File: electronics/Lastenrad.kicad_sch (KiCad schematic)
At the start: 42 parts, among them J1 Conn_Coaxial_Power, J2 Conn_Coaxial_Power, J3 Conn_Coaxial_Power

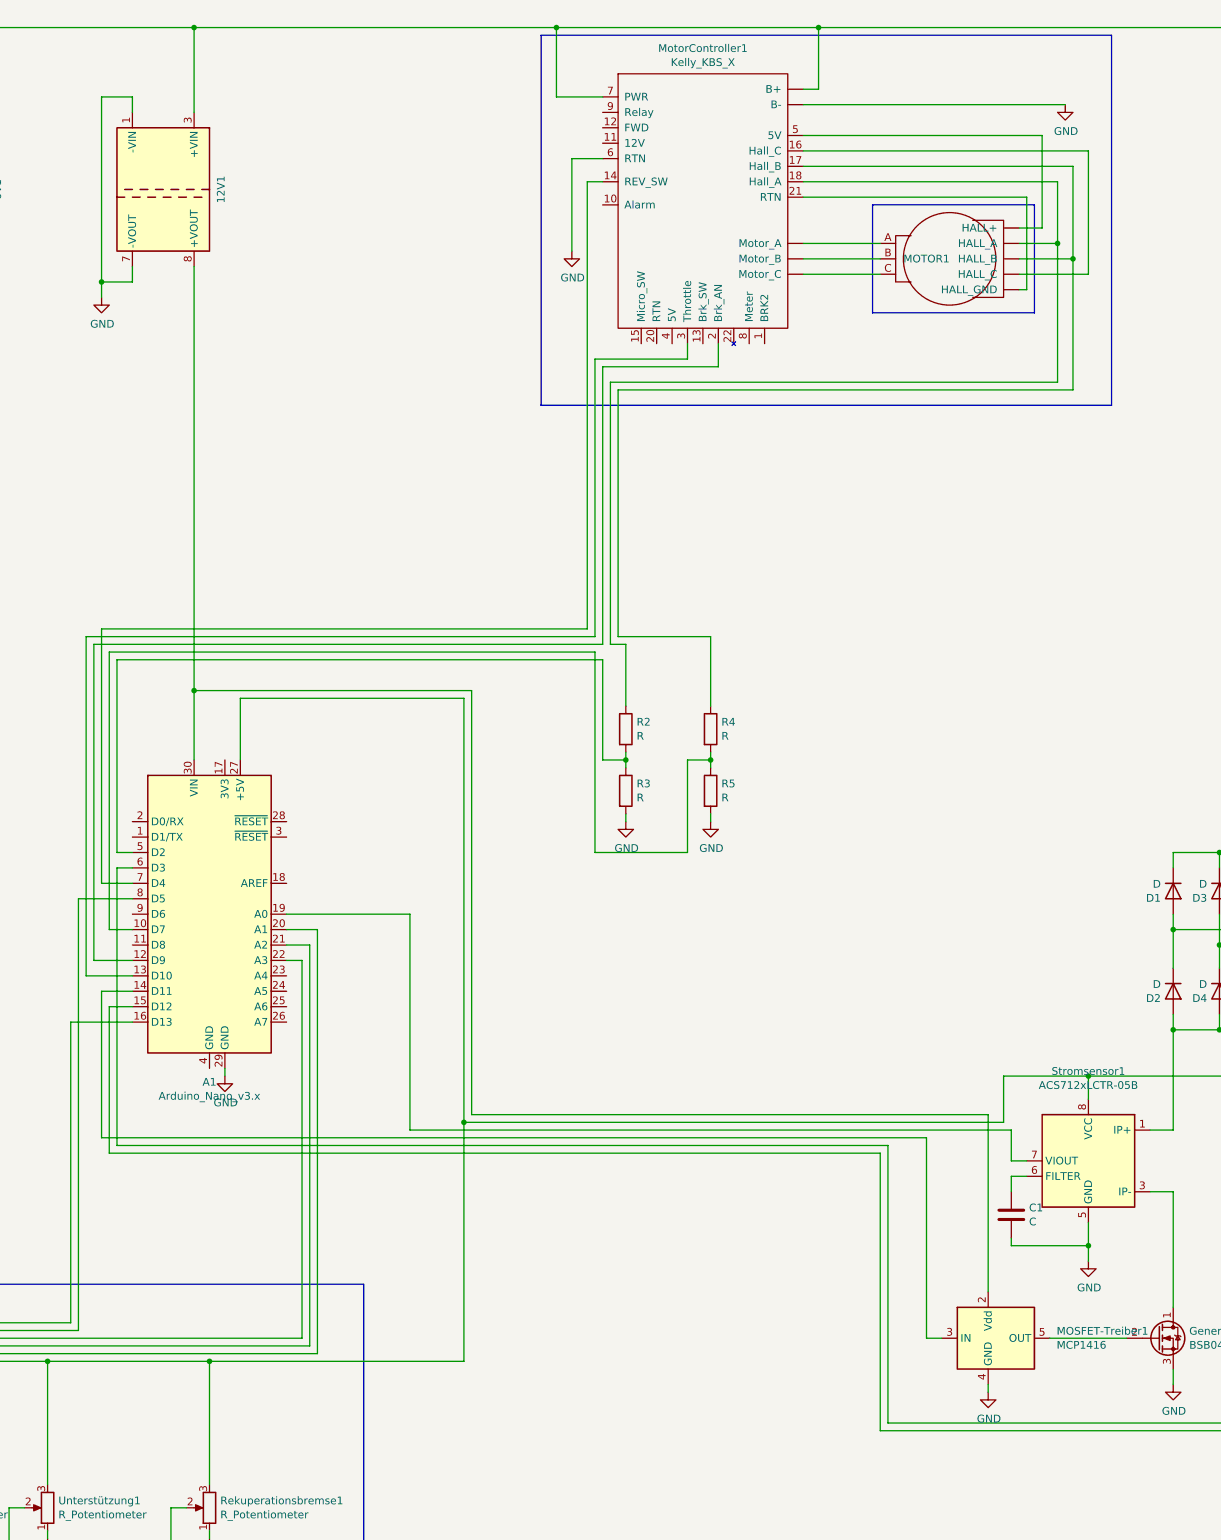
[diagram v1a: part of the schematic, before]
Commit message: Circuit diagram: Moved motor and motor controller
Slight adjustments to the positioning to make the connection between
different physical section more clear
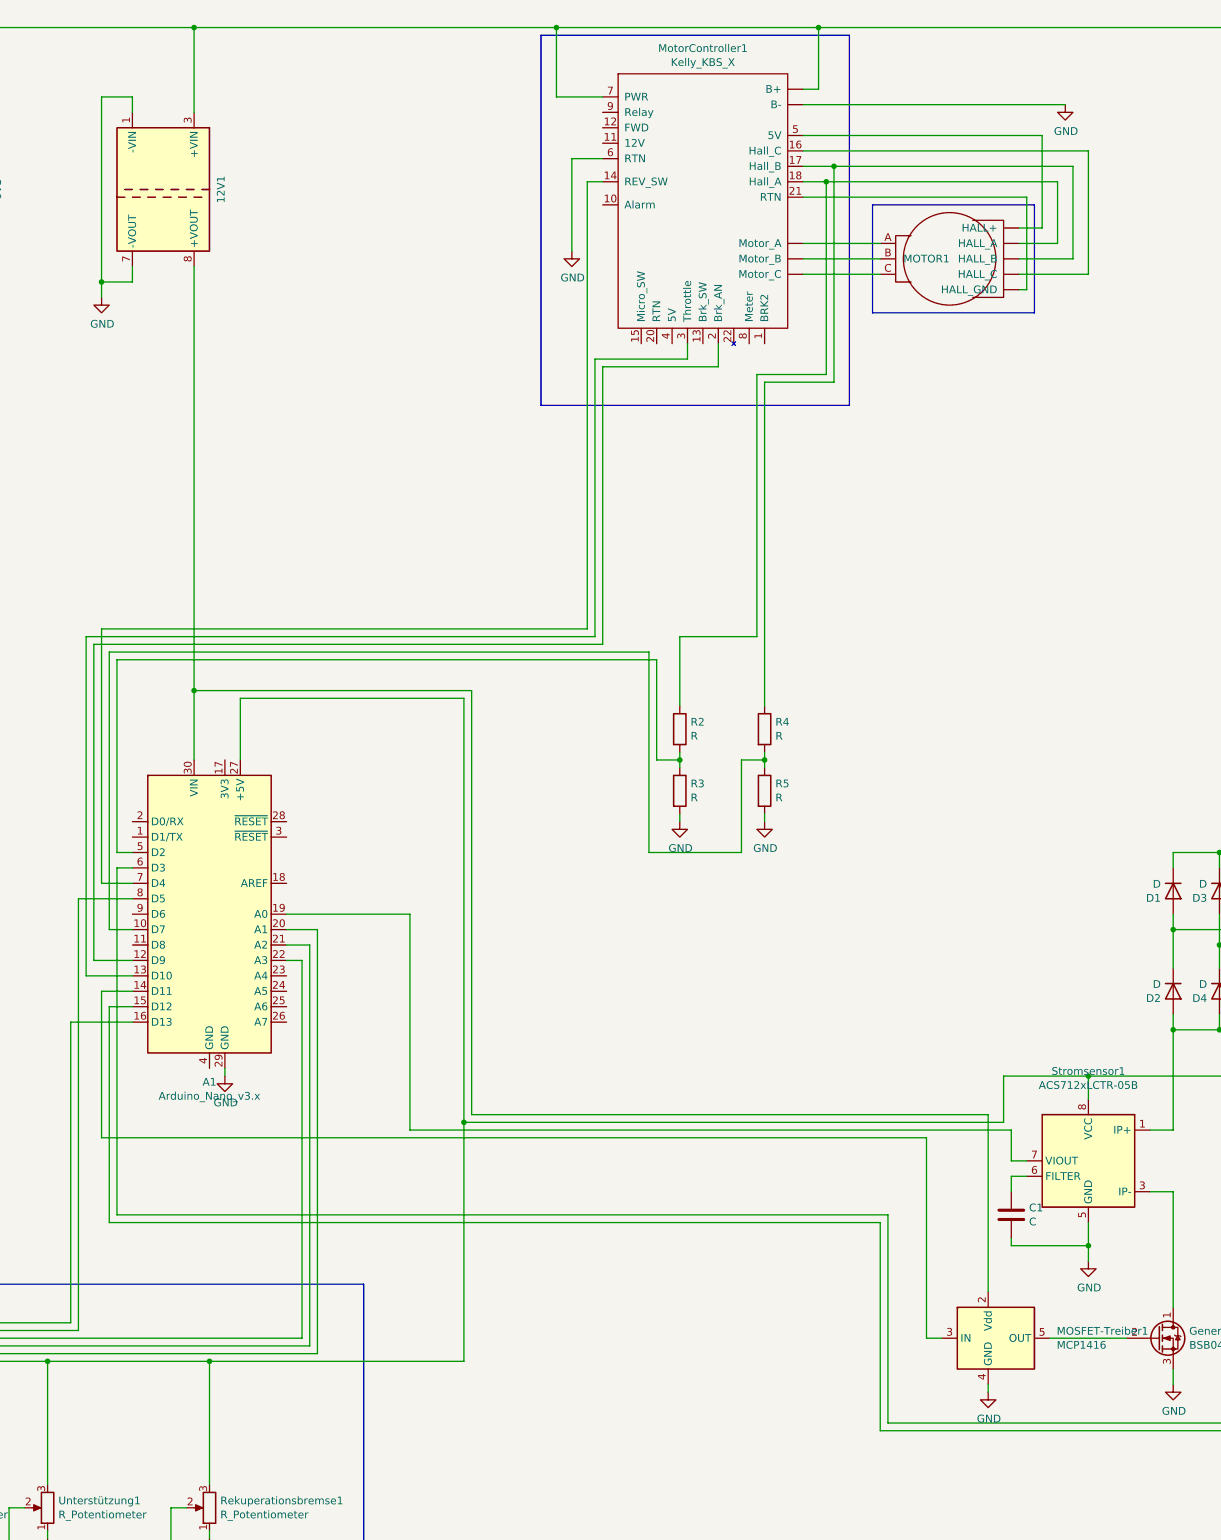
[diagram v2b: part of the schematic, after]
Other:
- moved on the sheet: R2, R3, R4, R5

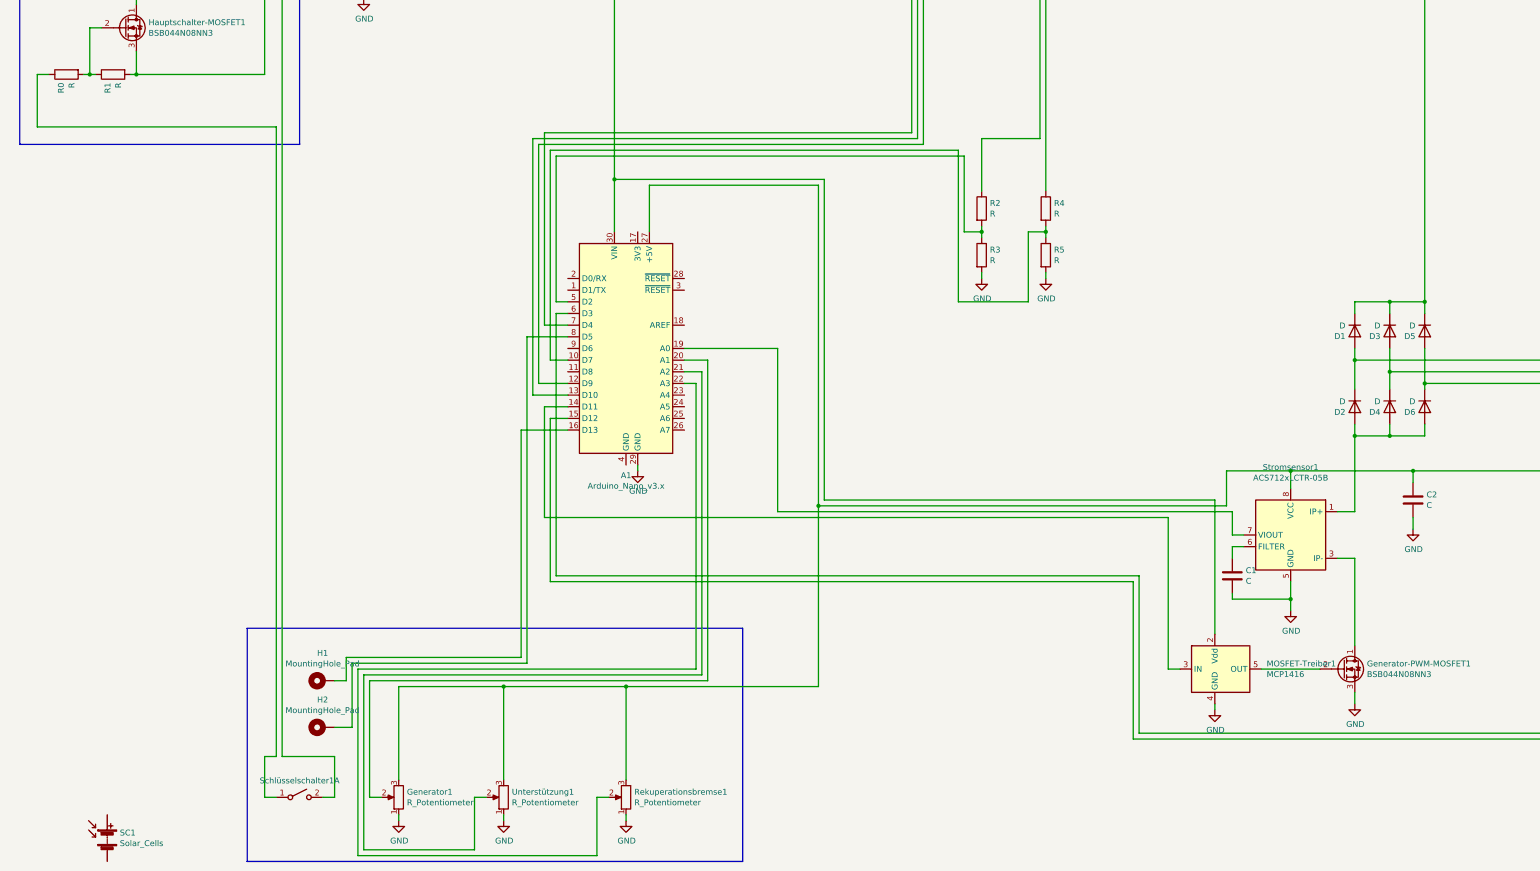
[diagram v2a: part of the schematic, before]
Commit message: Circuit diagram: Resistor values
My dad added sensible resistor values all around the circuit diagram
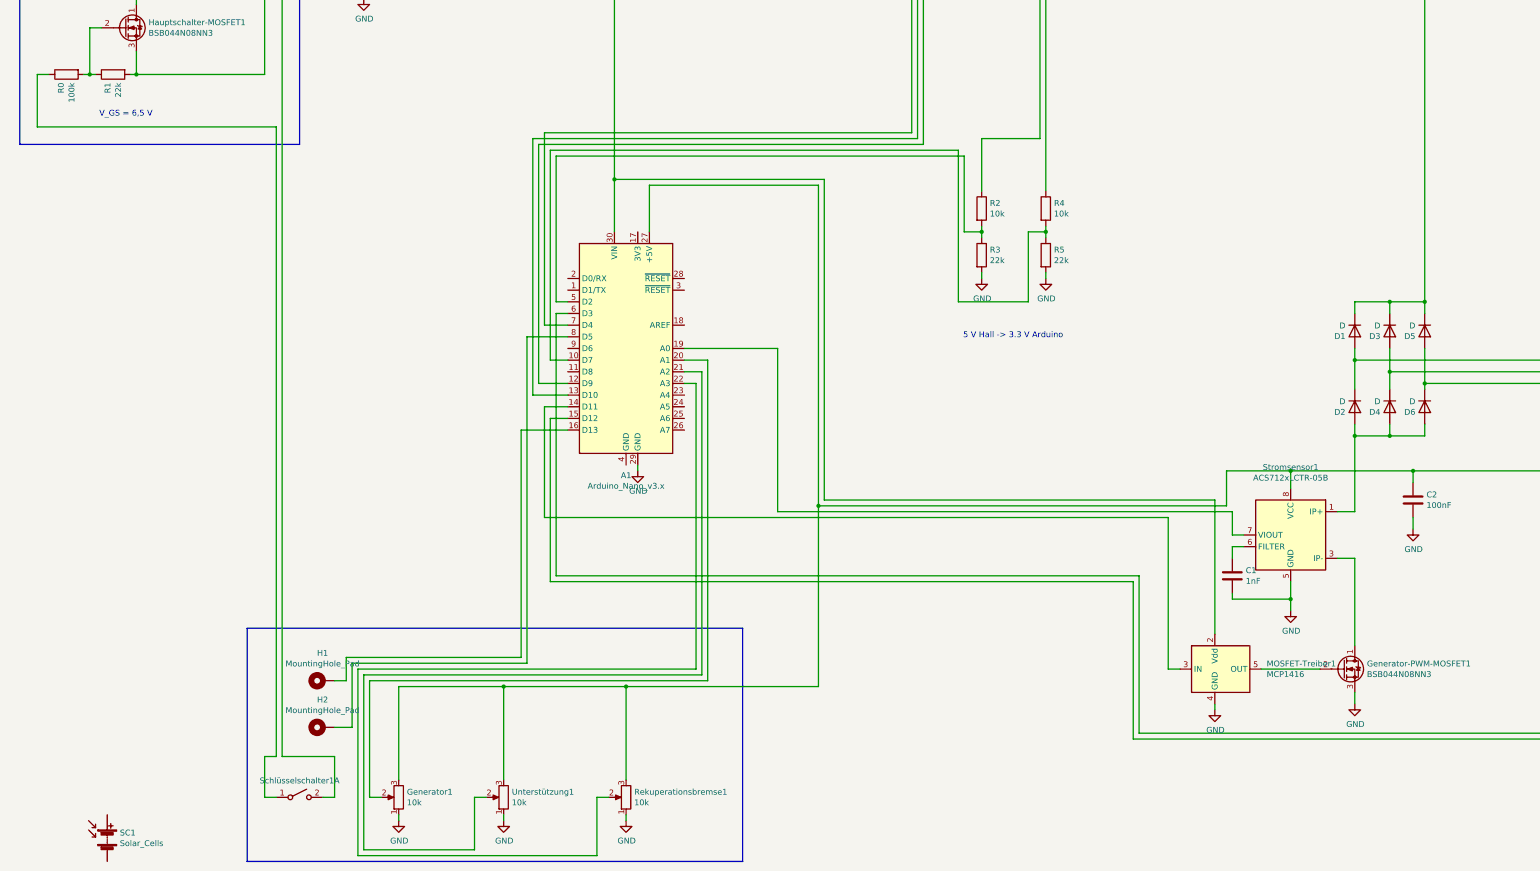
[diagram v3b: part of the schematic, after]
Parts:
- C1: value C -> 1nF
- C2: value C -> 100nF
- Generator1, Rekuperationsbremse1, Unterstützung1: value R_Potentiometer -> 10k
- R0: value R -> 100k
- R1, R3, R5: value R -> 22k
- R2, R4: value R -> 10k
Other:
- note added: "5 V Hall -> 3.3 V Arduino"
- note added: "V_GS = 6,5 V"
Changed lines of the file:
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@@
 	(generator_version "9.0")
 	(paper "A3")
+	(title_block
+		(date "2025-06-13")
+		(rev "PS1")
+	)
+	(text "V_GS = 6,5 V"
+		(exclude_from_sim no)
+		(at 38.354 115.316 0)
+		(effects
+			(font
+				(size 1.27 1.27)
+			)
+		)
+	)
+	(text "5 V Hall -> 3.3 V Arduino"
+		(exclude_from_sim no)
+		(at 231.648 163.576 0)
+		(effects
+			(font
+				(size 1.27 1.27)
+			)
+		)
+	)
 	(junction
 		(at 72.39 44.45)
@@
 			)
 		)
-		(property "Value" "R"
+		(property "Value" "22k"
 			(at 36.703 108.458 0)
 			(effects
@@
 			)
 		)
-		(property "Value" "R"
+		(property "Value" "10k"
 			(at 226.568 137.033 0)
 			(effects
@@
 			)
 		)
-		(property "Value" "R"
+		(property "Value" "22k"
 			(at 226.568 147.193 0)
 			(effects
@@
 			)
 		)
-		(property "Value" "R"
+		(property "Value" "100k"
 			(at 26.543 108.458 0)
 			(effects
@@
 			)
 		)
-		(property "Value" "R_Potentiometer"
+		(property "Value" "10k"
 			(at 99.568 265.303 0)
 			(effects
@@
 			)
 		)
-		(property "Value" "R_Potentiometer"
+		(property "Value" "10k"
 			(at 122.428 265.303 0)
 			(effects
@@
 			)
 		)
-		(property "Value" "R_Potentiometer"
+		(property "Value" "10k"
 			(at 149.098 265.303 0)
 			(effects
@@
 			)
 		)
-		(property "Value" "R"
+		(property "Value" "10k"
 			(at 240.538 137.033 0)
 			(effects
@@
 			)
 		)
-		(property "Value" "R"
+		(property "Value" "22k"
 			(at 240.538 147.193 0)
 			(effects
@@
 			)
 		)
-		(property "Value" "C"
+		(property "Value" "100nF"
 			(at 321.691 200.533 0)
 			(effects
@@
 			)
 		)
-		(property "Value" "C"
+		(property "Value" "1nF"
 			(at 282.321 217.043 0)
 			(effects
